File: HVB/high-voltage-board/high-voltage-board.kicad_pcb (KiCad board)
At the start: 2 copper layers, 158.5 x 96.5 mm, 69 parts, among them J1 Conn_01x23, J10 Conn_01x05, J11 HV-, J2 HECS, J3 HV+, J4 HV-, J5 HV+, J6 HV-, J7 Conn_01x02, J8 HV+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

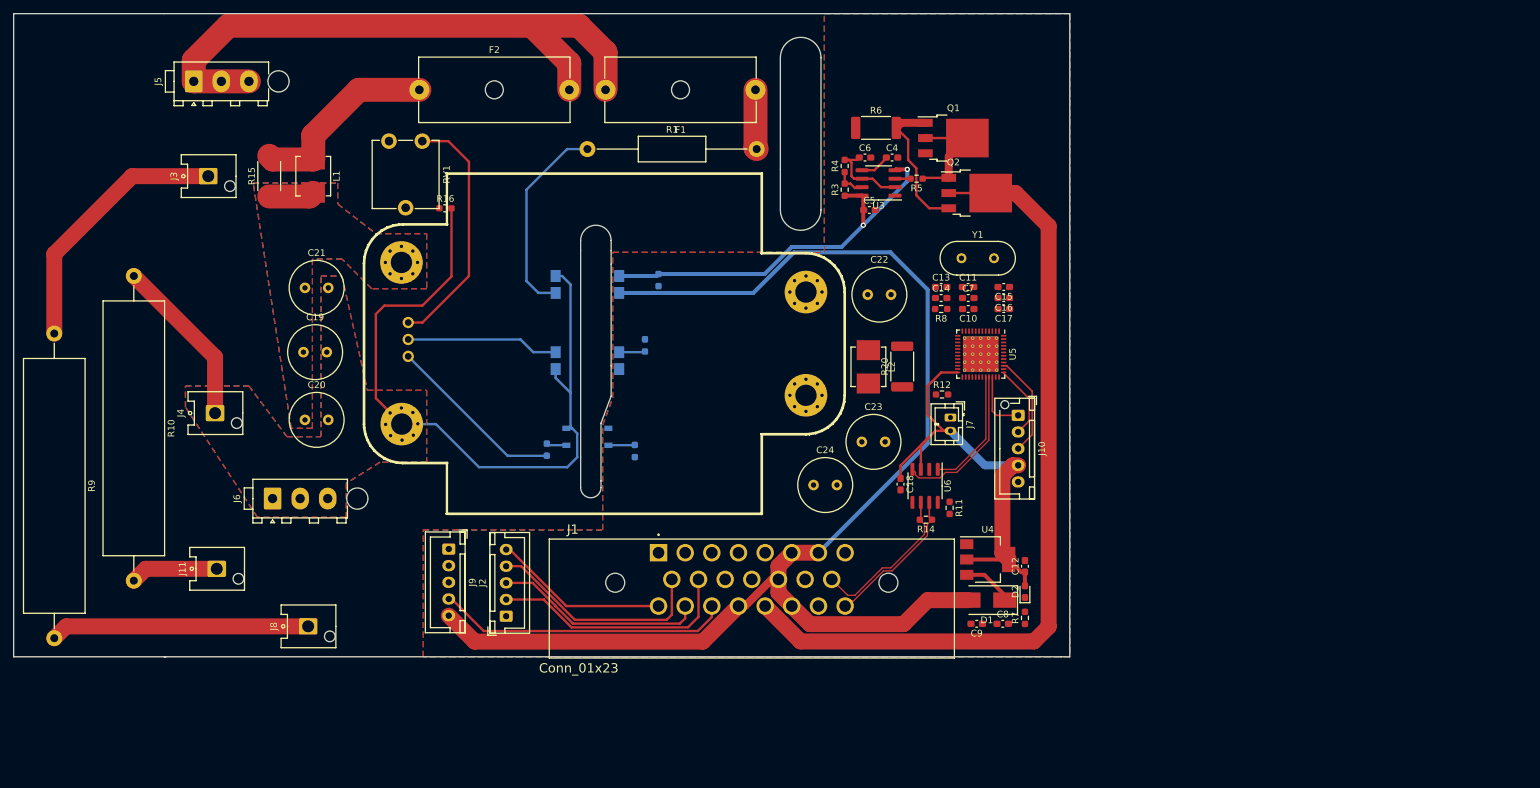
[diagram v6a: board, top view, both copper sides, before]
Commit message: adding corner cutout and updating layout
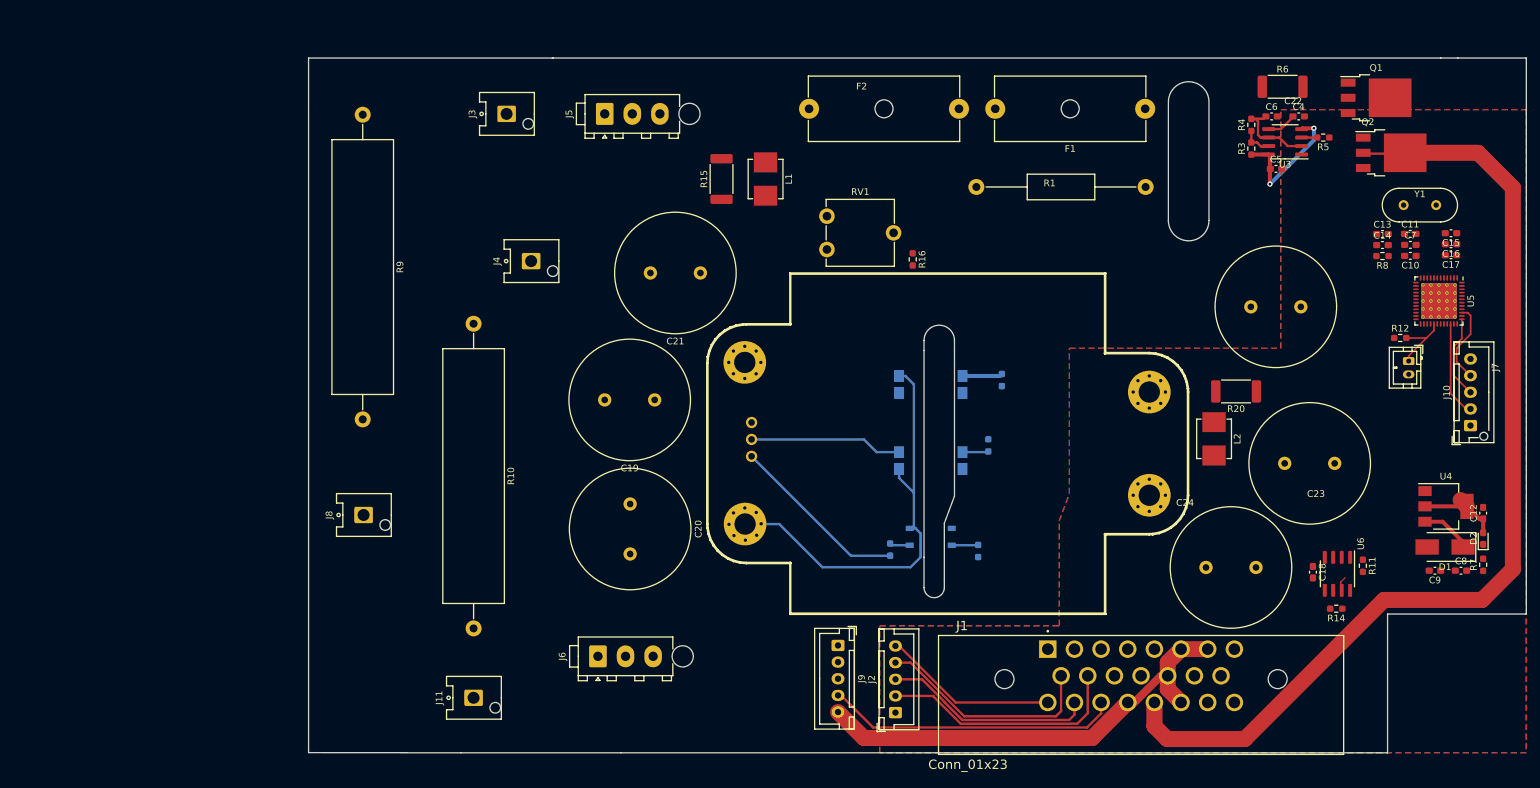
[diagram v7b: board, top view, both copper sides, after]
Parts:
- C19, C20, C21, C22, C23, C24: footprint Capacitor_THT:C_Radial_D8.0mm_H7.0mm_P3.50mm -> Capacitor_THT:C_Radial_D18.0mm_H35.5mm_P7.50mm
- moved R16 70.5 mm to (137.7, 69.9), turned to -90 degrees
- moved J7 69.3 mm to (212.2, 85.2)
- moved R12 69.3 mm to (210.9, 81.7)
- moved C9 69.2 mm to (216.1, 116.6)
- moved D1 69.2 mm to (217.6, 113.1)
- moved U5 69.2 mm to (216.7, 76.1)
- moved C12 69.2 mm to (223.3, 108.0)
- moved C8 69.2 mm to (220.0, 116.6)
- moved D2 69.2 mm to (223.3, 111.8)
- moved R7 69.2 mm to (223.3, 115.7)
- moved U4 69.2 mm to (217.7, 107.0)
- moved J10 67.9 mm to (221.4, 94.8), turned to 90 degrees
- moved L1 67.9 mm to (115.6, 57.8)
- moved R15 67.9 mm to (109.0, 57.8)
- moved RV1 67.7 mm to (124.8, 68.4), turned to 0 degrees
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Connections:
- J10 pad 1: A13_SWDIO -> +3V3
- J10 pad 2: A14_SWCLK -> A13_SWDIO
- J10 pad 3: B3_TRACESWO -> A14_SWCLK
- J10 pad 4: +3V3 -> B3_TRACESWO
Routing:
- net HV+: track 134.5 -> 0.00 mm
- net +12V: track 195.2 -> 68.6 mm
- net HV-: track 131.7 -> 64.1 mm
- net +3V3: track 70.5 -> 12.7 mm
- net Net-(J8-Pad1): track 38.8 -> 0.00 mm
- net /vicor/TRIM_HV: track 37.4 -> 0.00 mm
- net VCC: track 59.9 -> 26.1 mm
- net Net-(R1-Pad1): track 30.5 -> 0.00 mm
- net /vicor/HV+: track 29.2 -> 0.00 mm
- net /TSAL_GND: track 122.8 -> 150.6 mm
- net /controller/CAN_X_N: track 24.0 -> 0.00 mm
- net /CAN-: track 23.8 -> 0.00 mm
- net Net-(Q1-Pad1): track 21.7 -> 0.00 mm
- net /CAN+: track 22.2 -> 2.66 mm
- net /controller/CAN_X_P: track 18.4 -> 0.00 mm
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- removed copper zone on B.Cu, net HV-
- removed copper zone on F.Cu, net HV-
- removed copper zone on B.Cu, net Net-(C19-Pad1)
- removed copper zone on F.Cu, net Net-(C19-Pad1)
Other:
- board size 158.5 x 96.5 mm -> 182.8 x 104.3 mm

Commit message: Layout Trace Complete
completed layout of tracks. Still need to place silkscreens
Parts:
- R16: moved to B.Cu
- U5: footprint Package_DFN_QFN:QFN-48-1EP_7x7mm_P0.5mm_EP5.3x5.3mm_ThermalVias -> Package_DFN_QFN:QFN-48-1EP_7x7mm_P0.5mm_EP5.3x5.3mm
- moved C18 26.7 mm to (218.8, 100.5), turned to 180 degrees
- moved R14 22.2 mm to (220.2, 110.7)
- moved U6 22.2 mm to (220.3, 105.5)
- moved C12 21.1 mm to (202.4, 111.0)
- moved D1 20.6 mm to (197.4, 116.7), turned to -90 degrees
- moved R11 19.6 mm to (223.9, 109.9)
- moved C8 19.5 mm to (200.5, 116.0), turned to -90 degrees
- moved R7 18.6 mm to (206.8, 107.3), turned to 0 degrees
- moved C9 16.1 mm to (200.5, 112.5), turned to 90 degrees
- moved D2 13.8 mm to (210.3, 107.3), turned to 0 degrees
- moved U4 10.8 mm to (208.0, 111.8)
- moved R16 0.30 mm to (137.7, 69.6)
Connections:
- J1 pad 19: +12V -> unconnected-(J1-Pad19)
- J1 pad 20: /TSAL_GND -> +12V
- J1 pad 21: +12V -> /TSAL_GND
- J1 pad 8: unconnected-(J1-Pad8) -> GND
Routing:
- net +3V3: track 12.7 -> 251.1 mm, vias 0 -> 4
- net +12V: track 68.6 -> 215.7 mm
- net HV+: track 0.00 -> 131.3 mm
- net /DC_DC_FAULT: track 3.92 -> 98.3 mm, vias 0 -> 1
- net /DC_DC_EN: track 0.00 -> 78.9 mm, vias 0 -> 1
- net /CAN-: track 0.00 -> 58.8 mm
- net /CAN+: track 2.66 -> 58.7 mm
- net VCC: track 26.1 -> 78.2 mm
- net /vicor/TRIM_HV: track 0.00 -> 48.7 mm
- net Net-(R1-Pad1): track 0.00 -> 36.3 mm
- net /controller/CAN_X_P: track 0.00 -> 32.4 mm
- net /controller/CAN_X_N: track 0.00 -> 32.1 mm
- net Net-(Q1-Pad1): track 0.00 -> 24.1 mm
- net Net-(Q1-Pad2): track 0.00 -> 19.0 mm
- net HV-: track 64.1 -> 81.7 mm
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- added copper zone on B.Cu, net /DCDC_OUT
- added copper zone on F.Cu, net /DCDC_OUT
- added copper zone on B.Cu, net HV-
- added copper zone on F.Cu, net HV-
- added copper zone on B.Cu, net Net-(C19-Pad1)
- added copper zone on F.Cu, net Net-(C19-Pad1)
- added copper zone on B.Cu, net Net-(C22-Pad1)
- added copper zone on F.Cu, net Net-(C22-Pad1)
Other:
- board size 182.8 x 104.3 mm -> 181.6 x 105.4 mm
